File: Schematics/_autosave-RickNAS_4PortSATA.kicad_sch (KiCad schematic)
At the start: 10 parts, among them U1 SATA_Combined, U10 SATA_Power, U2 SATA_Data, U3 SATA_Power, U4 SATA_Combined, U5 SATA_Data, U6 SATA_Combined, U7 SATA_Data, U8 SATA_Combined, U9 SATA_Data

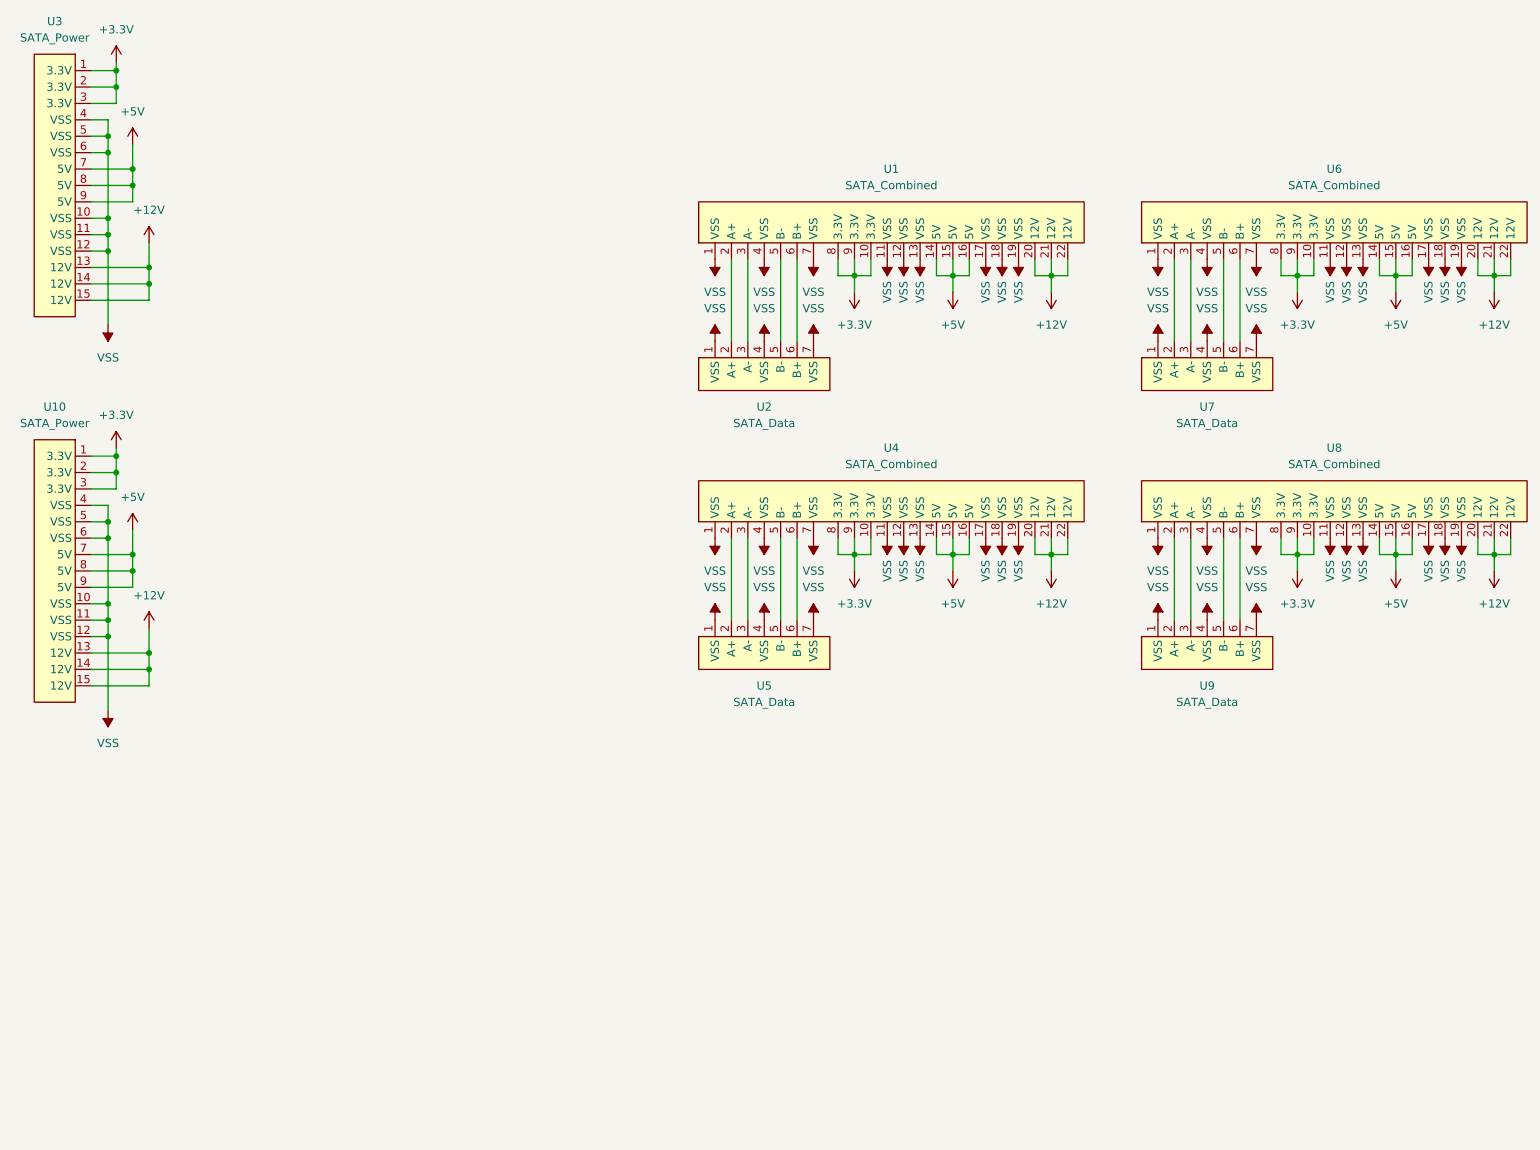
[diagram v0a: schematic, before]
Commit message: Ordering PCBs
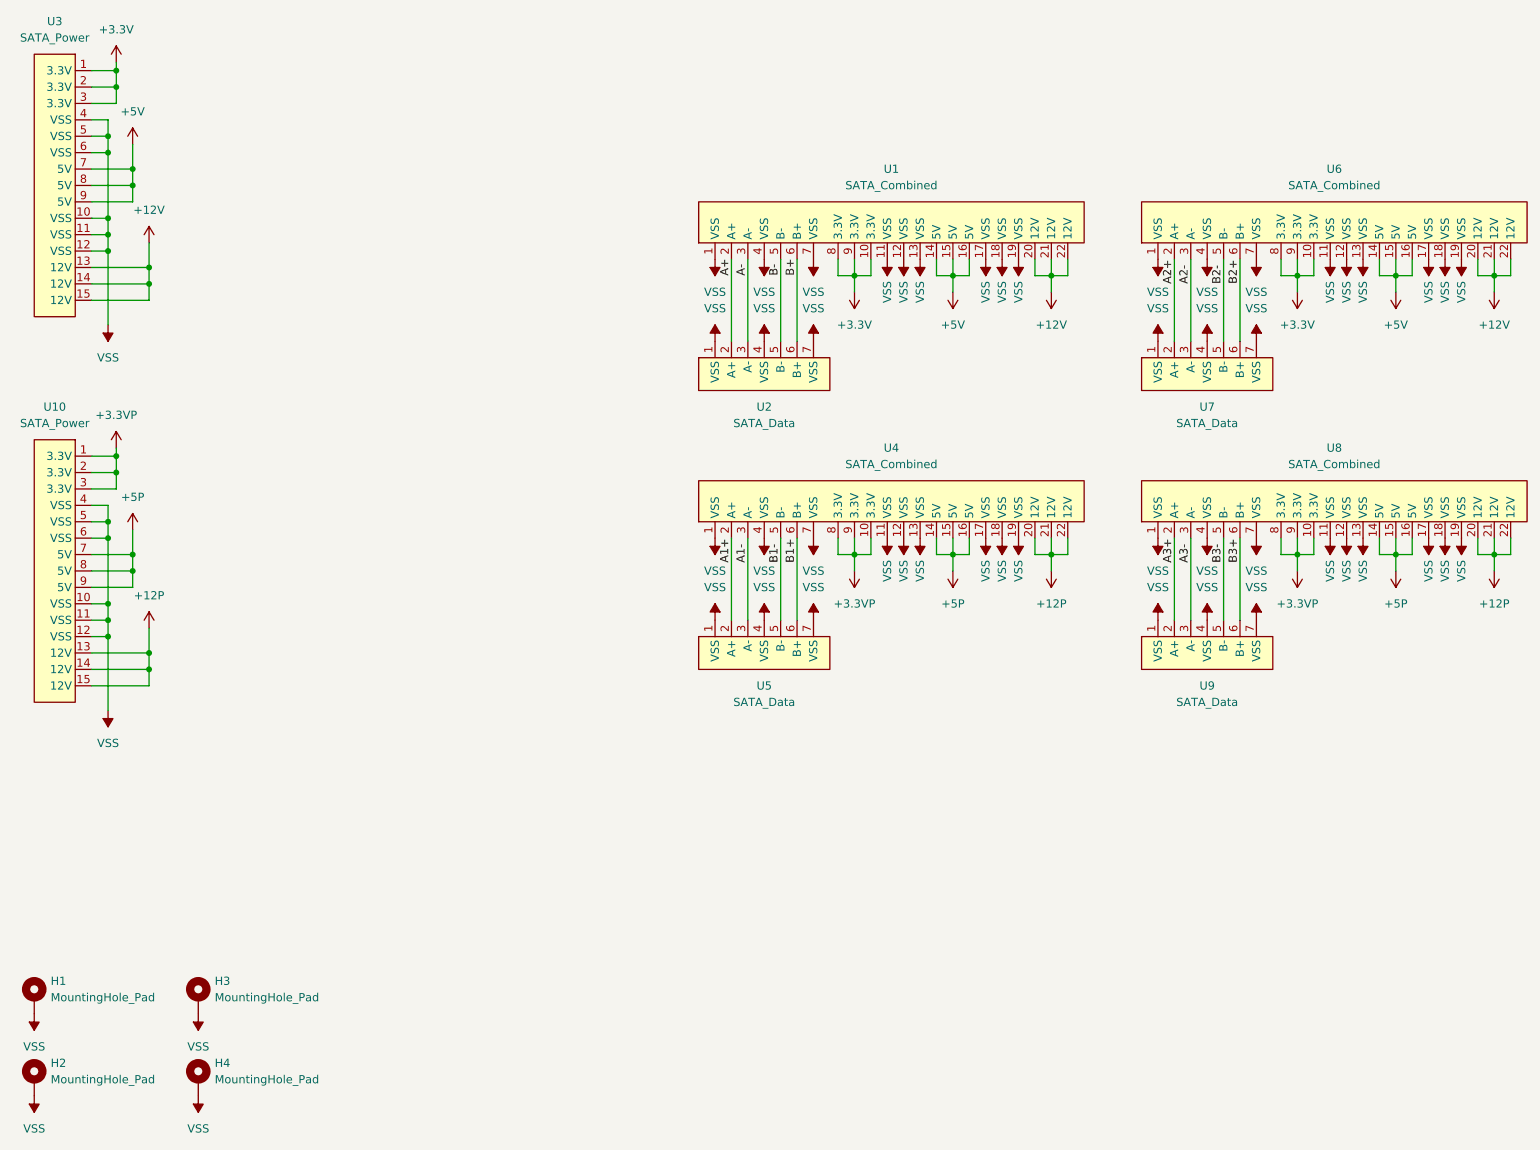
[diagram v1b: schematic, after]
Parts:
- added H1, H2, H3, H4: MountingHole_Pad, MountingHole:MountingHole_3.2mm_M3_DIN965_Pad, symbol Mechanical:MountingHole_Pad
- U1, U4, U6, U8: footprint UE-Connector:CONN22_1735284-3_TEC -> UE-Connector:CONN22_877811_MOL
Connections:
- net +12V: no longer U10.13 (12V), U10.14 (12V), U10.15 (12V), U4.20 (12V), U4.21 (12V), U4.22 (12V), U8.20 (12V), U8.21 (12V), U8.22 (12V)
- net +3.3V: no longer U10.1 (3.3V), U10.2 (3.3V), U10.3 (3.3V), U4.10 (3.3V), U4.8 (3.3V), U4.9 (3.3V), U8.10 (3.3V), U8.8 (3.3V), U8.9 (3.3V)
- net +5V: no longer U10.7 (5V), U10.8 (5V), U10.9 (5V), U4.14 (5V), U4.15 (5V), U4.16 (5V), U8.14 (5V), U8.15 (5V), U8.16 (5V)
- net VSS: now also H1.1, H2.1, H3.1, H4.1
- net A1+: now reaches U4.2 (A+), U5.2 (A+)
- net A1-: now reaches U4.3 (A-), U5.3 (A-)
- net B1-: now reaches U4.5 (B-), U5.5 (B-)
- net B1+: now reaches U4.6 (B+), U5.6 (B+)
- net A2+: now reaches U6.2 (A+), U7.2 (A+)
- net A2-: now reaches U6.3 (A-), U7.3 (A-)
- net B2-: now reaches U6.5 (B-), U7.5 (B-)
- net B2+: now reaches U6.6 (B+), U7.6 (B+)
- net A3+: now reaches U8.2 (A+), U9.2 (A+)
- net A3-: now reaches U8.3 (A-), U9.3 (A-)
- net B3-: now reaches U8.5 (B-), U9.5 (B-)
- net B3+: now reaches U8.6 (B+), U9.6 (B+)
- net A+: now reaches U1.2 (A+), U2.2 (A+)
- net A-: now reaches U1.3 (A-), U2.3 (A-)
- net B-: now reaches U1.5 (B-), U2.5 (B-)
- net B+: now reaches U1.6 (B+), U2.6 (B+)
- new net +12P: U10.13 (12V), U10.14 (12V), U10.15 (12V), U4.20 (12V), U4.21 (12V), U4.22 (12V), U8.20 (12V), U8.21 (12V), U8.22 (12V)
- new net +3.3VP: U10.1 (3.3V), U10.2 (3.3V), U10.3 (3.3V), U4.10 (3.3V), U4.8 (3.3V), U4.9 (3.3V), U8.10 (3.3V), U8.8 (3.3V), U8.9 (3.3V)
- new net +5P: U10.7 (5V), U10.8 (5V), U10.9 (5V), U4.14 (5V), U4.15 (5V), U4.16 (5V), U8.14 (5V), U8.15 (5V), U8.16 (5V)
